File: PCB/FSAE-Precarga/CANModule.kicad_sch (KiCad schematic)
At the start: 5 parts, among them J2 Conn_01x04, U8 ISO1044BD

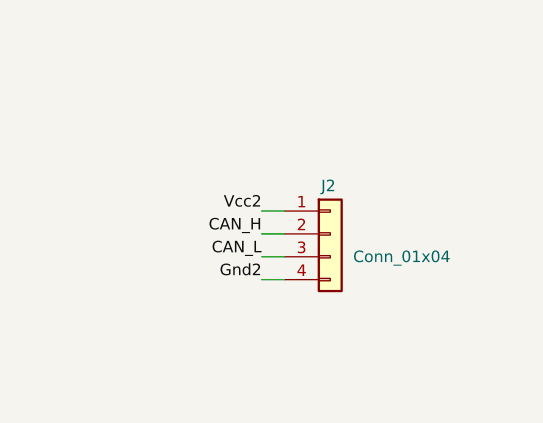
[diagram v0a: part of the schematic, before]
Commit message: Version avanzada de la placa de Precarga
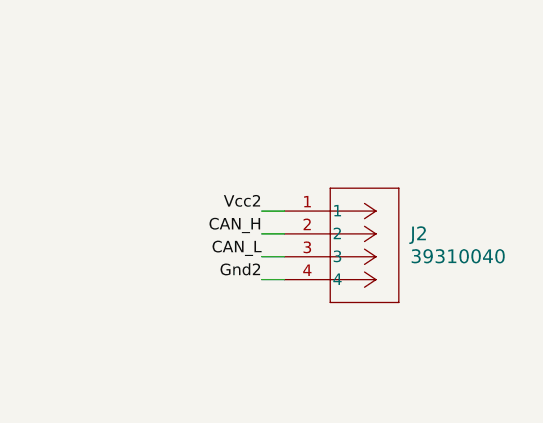
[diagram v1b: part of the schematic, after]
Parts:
- removed J2: Conn_01x04, GeneratedConnector:Molex_Mini50, symbol Connector_Generic:Conn_01x04
- added J2: 39310040, CONN_SD-5566-002_04_MOL, symbol 2026-08-15_23-43-52:39310040
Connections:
- net CAN_H: now also J2.2
- net CAN_L: now also J2.3
- net Gnd2: now also J2.4
- net Vcc2: now also J2.1
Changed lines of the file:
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@@
+	)
+	(symbol
+		(lib_id "2026-08-15_23-43-52:39310040")
+		(at 218.44 57.15 0)
+		(unit 1)
+		(exclude_from_sim no)
+		(in_bom yes)
+		(on_board yes)
+		(dnp no)
+		(fields_autoplaced yes)
+		(property "Reference" "J2"
+			(at 232.41 59.6899 0)
+			(effects
+				(font
+					(size 1.524 1.524)
+				)
+				(justify left)
+			)
+		)
+		(property "Value" "39310040"
+			(at 232.41 62.2299 0)
+			(effects
+				(font
+					(size 1.524 1.524)
+				)
+				(justify left)
+			)
+		)
+		(property "Footprint" "CONN_SD-5566-002_04_MOL"
+			(at 218.44 57.15 0)
+			(effects
+				(font
+					(size 1.27 1.27)
+					(italic yes)
+				)
+				(hide yes)
+			)
+		)
+		(property "Datasheet" "https://www.molex.com/en-us/products/part-detail-pdf/39310040?display=pdf"
+			(at 218.44 57.15 0)
+			(effects
+				(font
+					(size 1.27 1.27)
+					(italic yes)
+				)
+				(hide yes)
+			)
+		)
+		(property "Description" ""
+			(at 218.44 57.15 0)
+			(effects
+				(font
+					(size 1.27 1.27)
+				)
+				(hide yes)
+			)
+		)
+		(pin "2"
+		)
+		(pin "4"
+		)
+		(pin "3"
+		)
+		(pin "1"
+		)
+		(instances
+			(project ""
+				(path "/794055b5-0f32-485f-b098-05722541fd08/47c2bb38-7e57-46d4-86d8-77f86c77d7af"
+					(reference "J2")
+					(unit 1)
+				)
+			)
+		)
 	)
 	(symbol
@@
 					(unit 1)
 				)
-			)
-		)
-	)
-	(symbol
-		(lib_id "Connector_Generic:Conn_01x04")
-		(at 223.52 59.69 0)
-		(unit 1)
-		(exclude_from_sim no)
-		(in_bom yes)
-		(on_board yes)
-		(dnp no)
-		(property "Reference" "J2"
-			(at 222.504 54.356 0)
-			(effects
-				(font
-					(size 1.27 1.27)
-				)
-				(justify left)
-			)
-		)
-		(property "Value" "Conn_01x04"
-			(at 226.06 62.2299 0)
-			(effects
-				(font
-					(size 1.27 1.27)
-				)
-				(justify left)
-			)
-		)
-		(property "Footprint" "GeneratedConnector:Molex_Mini50"
-			(at 223.52 59.69 0)
-			(effects
-				(font
-					(size 1.27 1.27)
-				)
-				(hide yes)
-			)
-		)
-		(property "Datasheet" "~"
-			(at 223.52 59.69 0)
-			(effects
-				(font
-					(size 1.27 1.27)
-				)
-				(hide yes)
-			)
-		)
-		(property "Description" "Generic connector, single row, 01x04, script generated (kicad-library-utils/schlib/autogen/connector/)"
-			(at 223.52 59.69 0)
-			(effects
-				(font
-					(size 1.27 1.27)
-				)
-				(hide yes)
-			)
-		)
-		(property "PaginaProveedor" ""
-			(at 223.52 59.69 0)
-			(effects
-				(font
-					(size 1.27 1.27)
-				)
-				(hide yes)
-			)
-		)
-		(property "JLCPart" ""
-			(at 223.52 59.69 0)
-			(effects
-				(font
-					(size 1.27 1.27)
-				)
-				(hide yes)
-			)
-		)
-		(pin "1"
-		)
-		(pin "4"
-		)
-		(pin "3"
-		)
-		(pin "2"
-		)
-		(instances
-			(project ""
-				(path "/794055b5-0f32-485f-b098-05722541fd08/47c2bb38-7e57-46d4-86d8-77f86c77d7af"
-					(reference "J2")
-					(unit 1)
-				)

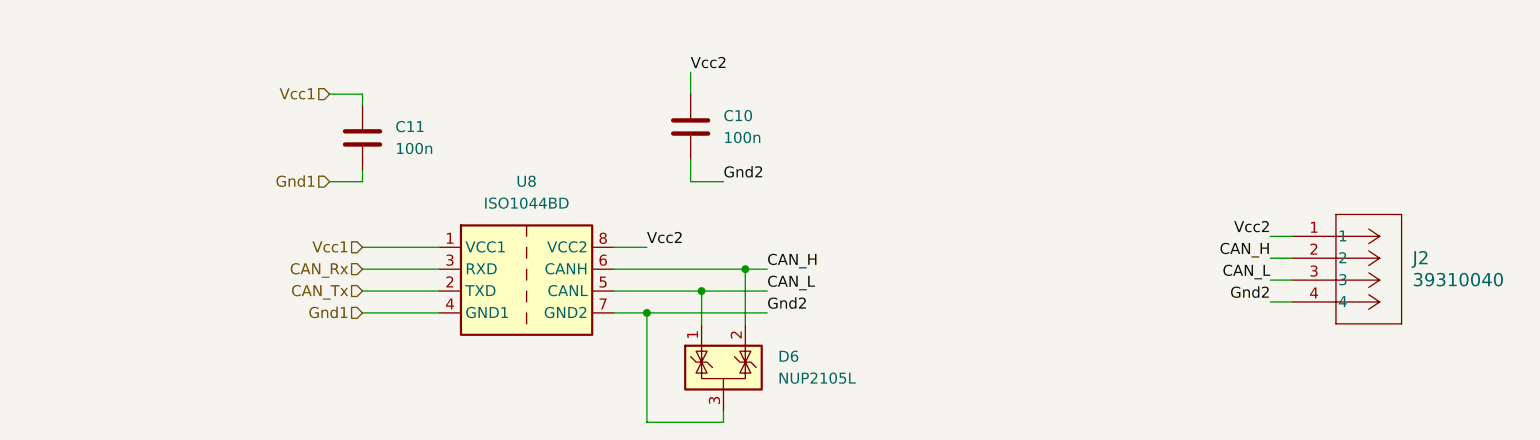
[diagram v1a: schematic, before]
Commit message: Agrego correcciones/agregados placa precarga
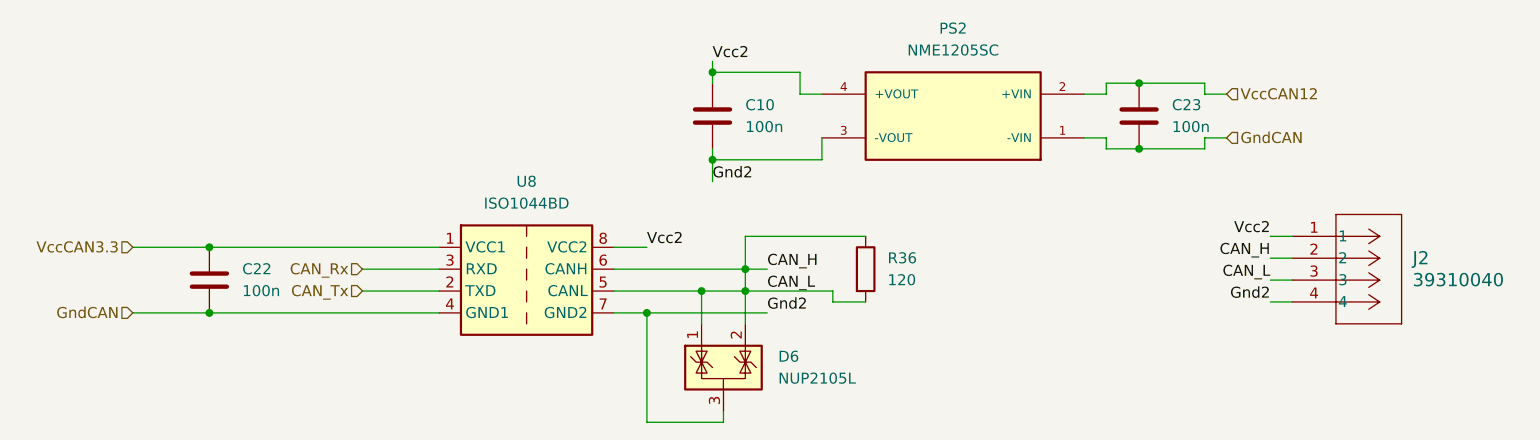
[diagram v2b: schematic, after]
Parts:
- removed C11: 100n, Capacitor_SMD:C_0603_1608Metric, symbol Device:C
- added C22, C23: 100n, Capacitor_SMD:C_0603_1608Metric, symbol Device:C
- added PS2: NME1205SC, Mis_Huellas:CONV_NME1205SC, symbol NME1205SC:NME1205SC
- added R36: 120, Resistor_SMD:R_0805_2012Metric, symbol Device:R
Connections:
- net CAN_L is gone; now on net CAN_H: D6.1 (K), J2.3, U8.5 (CANL)
- net CAN_H: now also R36.1, R36.2
- net Gnd2: now also PS2.3 (-VOUT)
- net Vcc2: now also PS2.4 (+VOUT)
- net Gnd1 renamed GndCAN
- net GndCAN: now also C22.2, C23.2, PS2.1 (-VIN)
- net Vcc1 renamed VccCAN3.3
- net VccCAN3.3: now also C22.1
- new net VccCAN12: C23.1, PS2.2 (+VIN)
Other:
- moved on the sheet: C10
